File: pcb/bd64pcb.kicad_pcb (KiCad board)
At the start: 2 copper layers, 266.7 x 95.2 mm, 245 parts, among them J1 USB_C_Receptacle_USB2.0, SW1 SW_Push, U1 ATmega32U4-MU, U2 MCP23017_ML, U3 IS31FL3733-QF, Y1 16MHz

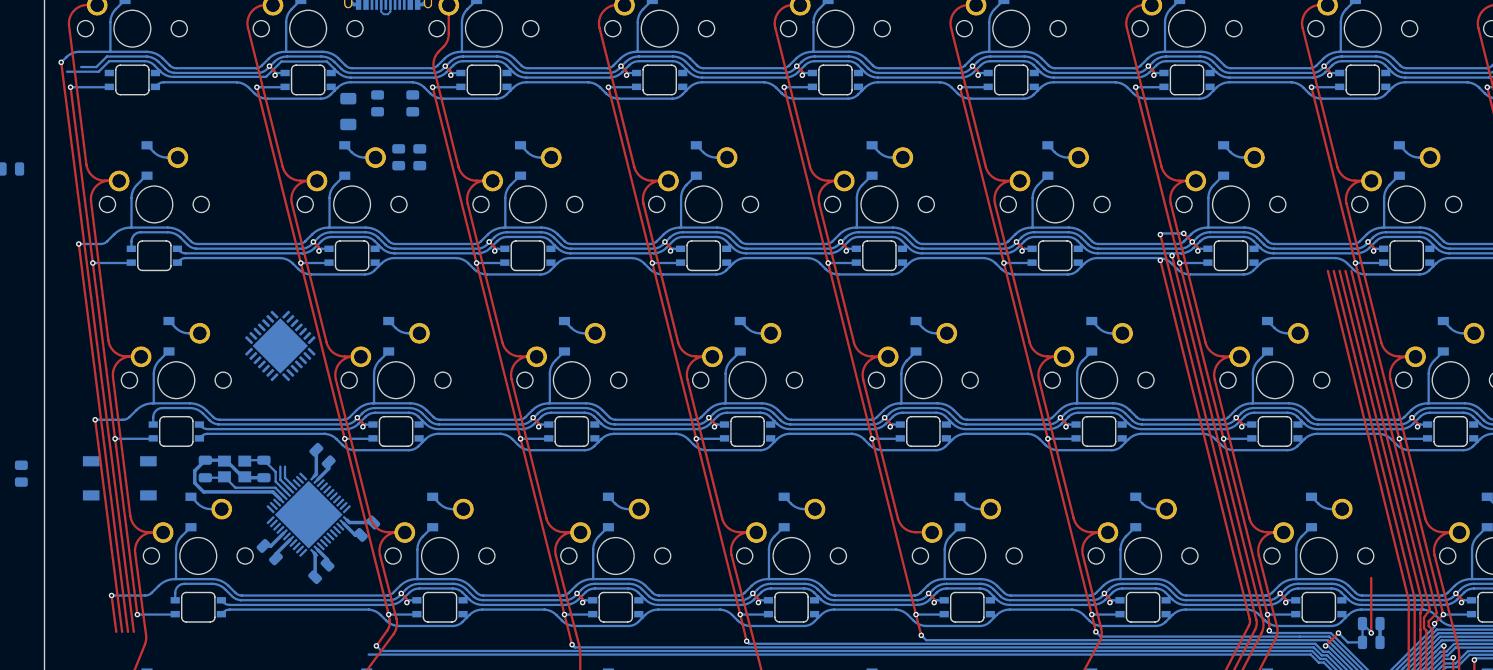
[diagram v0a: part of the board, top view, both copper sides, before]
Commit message: IIC lines from ISSI
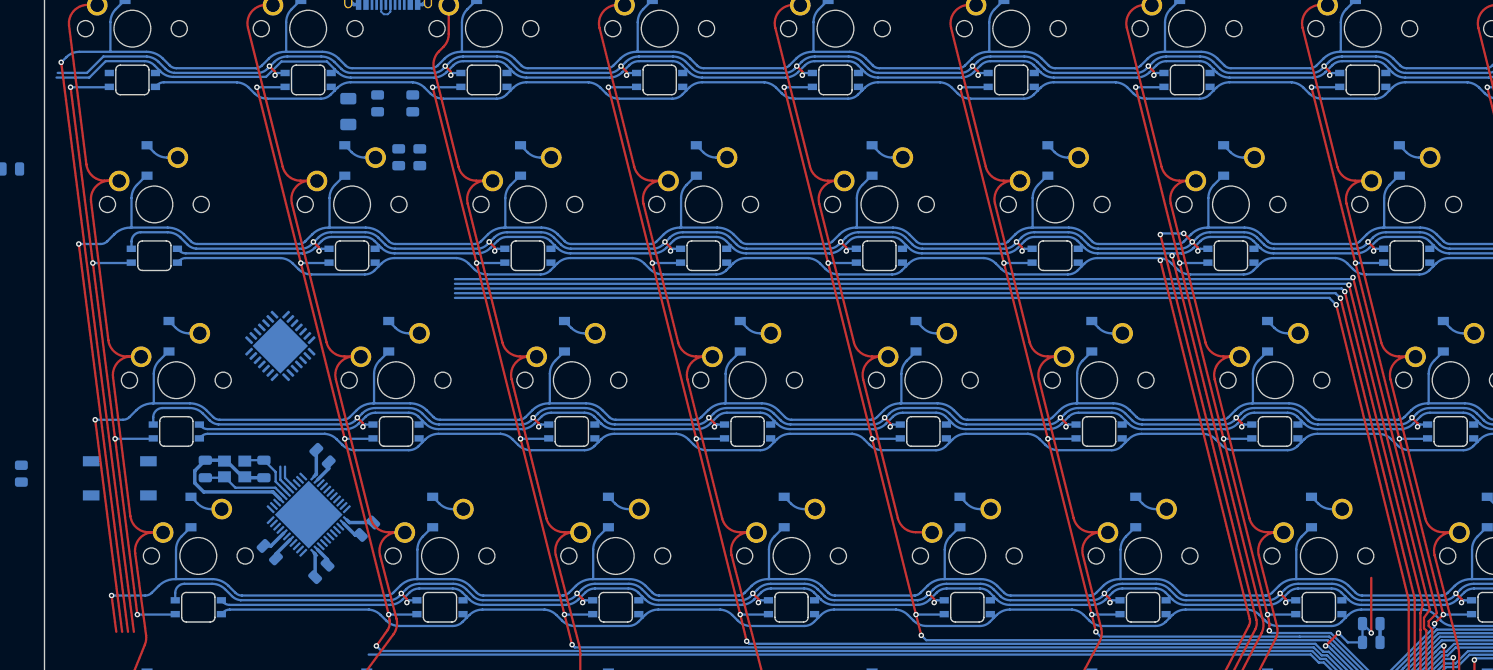
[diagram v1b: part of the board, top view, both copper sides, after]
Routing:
- net SDA: track 57.8 -> 154.4 mm, vias 1 -> 2
- net SCL: track 57.5 -> 152.9 mm, vias 1 -> 2
- net INTB: track 55.5 -> 149.8 mm, vias 1 -> 2
- net SDB: track 55.8 -> 149.0 mm, vias 1 -> 2
- net IICRST: track 56.3 -> 148.3 mm, vias 1 -> 2
- net SW3: track 342.3 -> 345.1 mm
- net SW1: track 322.1 -> 323.5 mm

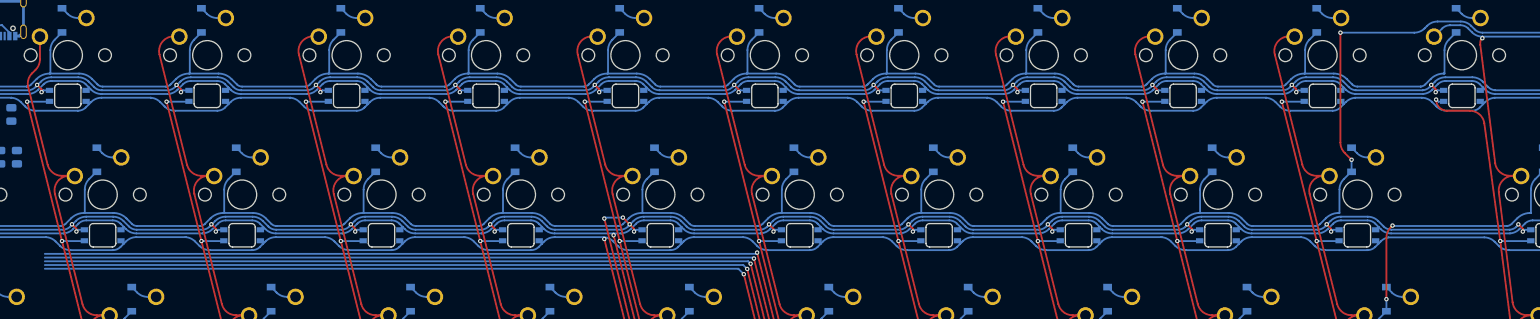
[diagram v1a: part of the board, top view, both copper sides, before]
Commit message: routing switch cols
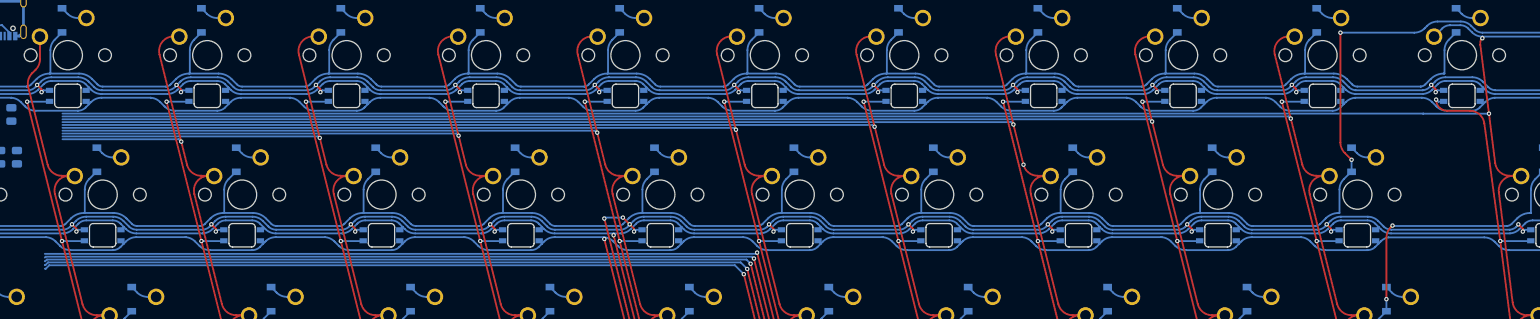
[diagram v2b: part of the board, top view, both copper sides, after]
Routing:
- net col12: track 89.9 -> 284.8 mm, vias 1 -> 2
- net col11: track 113.1 -> 281.1 mm, vias 1 -> 2
- net col10: track 109.0 -> 258.0 mm, vias 1 -> 2
- net col9: track 104.1 -> 234.2 mm, vias 1 -> 3
- net col8: track 99.5 -> 210.5 mm, vias 1 -> 2
- net col7: track 93.7 -> 185.8 mm, vias 0 -> 1
- net col6: track 94.5 -> 167.7 mm, vias 0 -> 1
- net col5: track 94.6 -> 148.8 mm, vias 0 -> 1
- net col4: track 72.5 -> 107.7 mm, vias 0 -> 1
- net col3: track 101.8 -> 118.1 mm, vias 1 -> 2

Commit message: finna delete mcp
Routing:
- net SW9: track 400.4 -> 416.7 mm
- net SW8: track 366.4 -> 381.1 mm, vias 2 -> 4
- net SW7: track 370.5 -> 378.2 mm, vias 2 -> 4
- net SW12: track 380.4 -> 385.7 mm, vias 32 -> 33
- net SW3: track 345.1 -> 348.0 mm, vias 30 -> 33
- net SW6: track 424.3 -> 426.2 mm, vias 33 -> 34
- net SW1: track 323.5 -> 321.8 mm, vias 0 -> 1
- net SW5: track 390.8 -> 392.1 mm, vias 2 -> 3
- net SW2: track 309.9 -> 309.1 mm, vias 0 -> 1
- net SW4: track 393.4 -> 394.2 mm, vias 2 -> 3

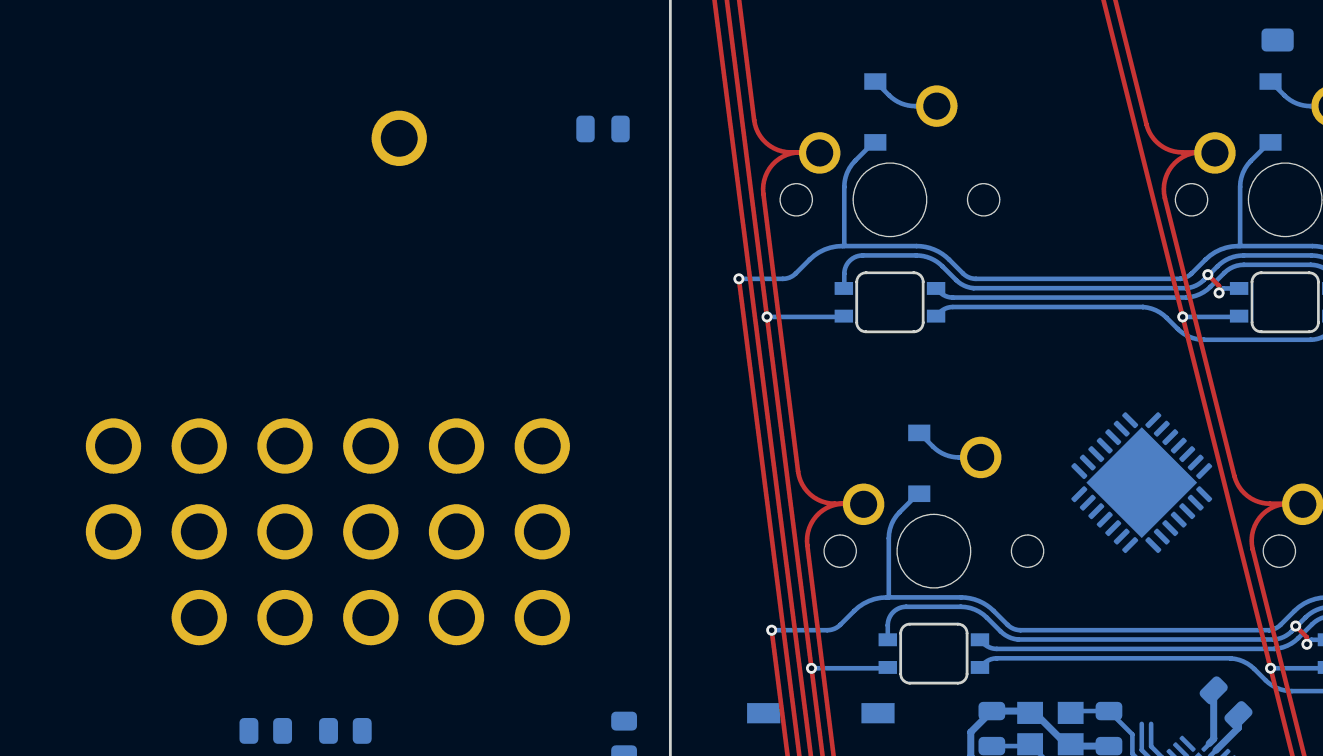
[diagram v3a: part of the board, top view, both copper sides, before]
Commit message: mcp delet
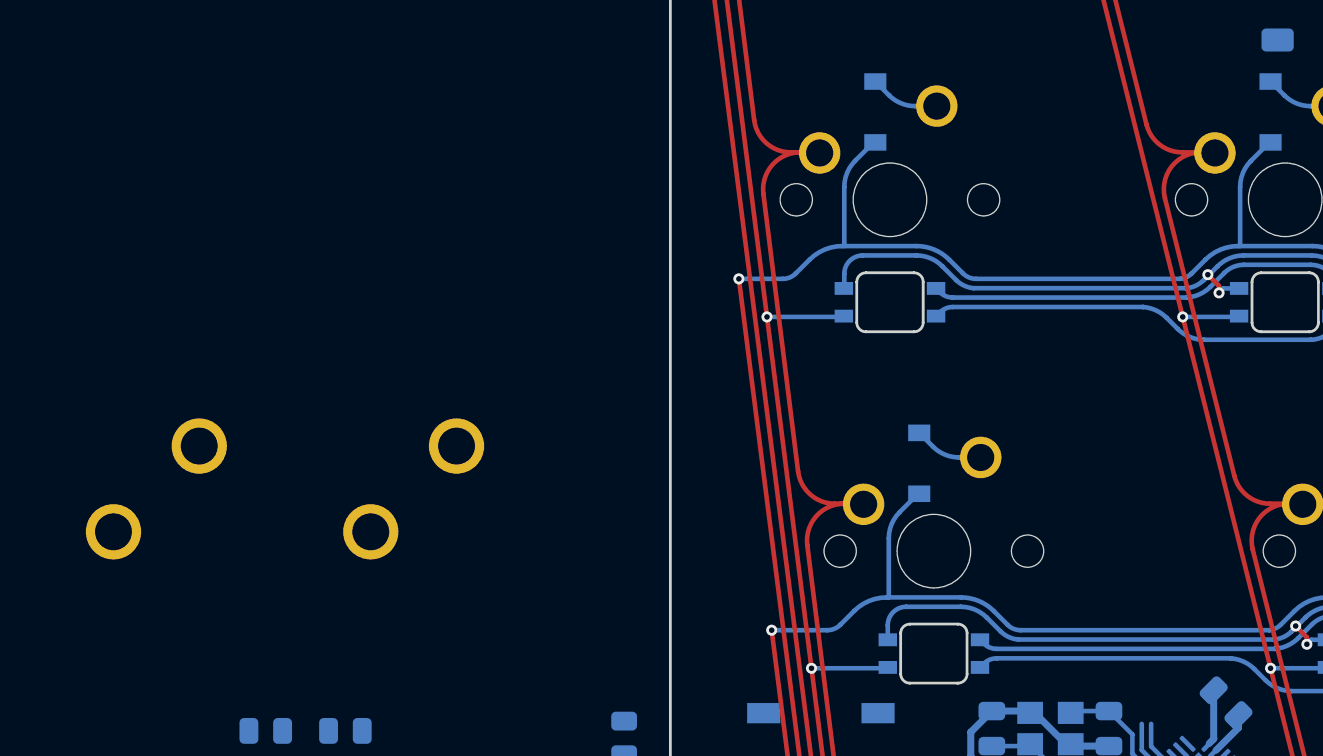
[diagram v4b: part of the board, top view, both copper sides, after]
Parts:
- removed C8: 1uF, Capacitor_SMD:C_0805_2012Metric
- removed TP1, TP10, TP11, TP12, TP13, TP14, TP15, TP16, TP17, TP18, TP2, TP4, TP6, TP8: TestPoint, TestPoint:TestPoint_Plated_Hole_D2.0mm
- removed U2: MCP23017_ML, Package_DFN_QFN:QFN-28-1EP_6x6mm_P0.65mm_EP4.25x4.25mm
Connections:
- U1 pad 21: unconnected-(U1-Pad21) -> row0
- U1 pad 22: unconnected-(U1-Pad22) -> row2
- U1 pad 25: unconnected-(U1-Pad25) -> row1
- U1 pad 26: unconnected-(U1-Pad26) -> row3
- U1 pad 27: unconnected-(U1-Pad27) -> row4

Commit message: sw1-3 routed
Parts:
- TP3, TP5, TP7, TP9: footprint TestPoint:TestPoint_Plated_Hole_D2.0mm -> TestPoint:TestPoint_Pad_D1.5mm
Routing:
- net SW2: track 309.1 -> 508.7 mm, vias 1 -> 4
- net SW1: track 321.8 -> 514.8 mm, vias 1 -> 4
- net SW3: track 348.0 -> 536.5 mm, vias 33 -> 36
- net CS1: track 183.4 -> 213.4 mm, vias 4 -> 5
- net row4: track 351.0 -> 350.5 mm, vias 2 -> 3

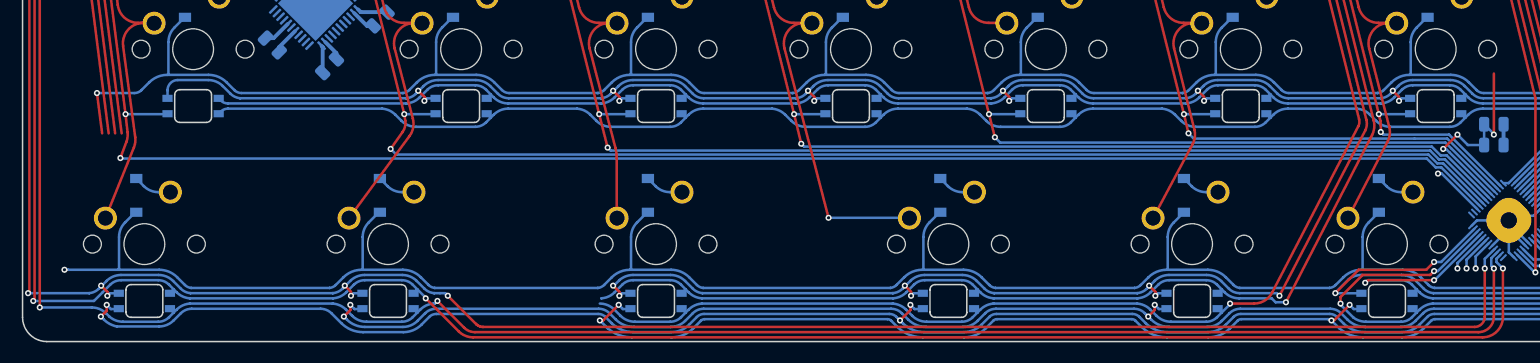
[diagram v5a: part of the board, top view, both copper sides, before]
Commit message: led SW pins routed
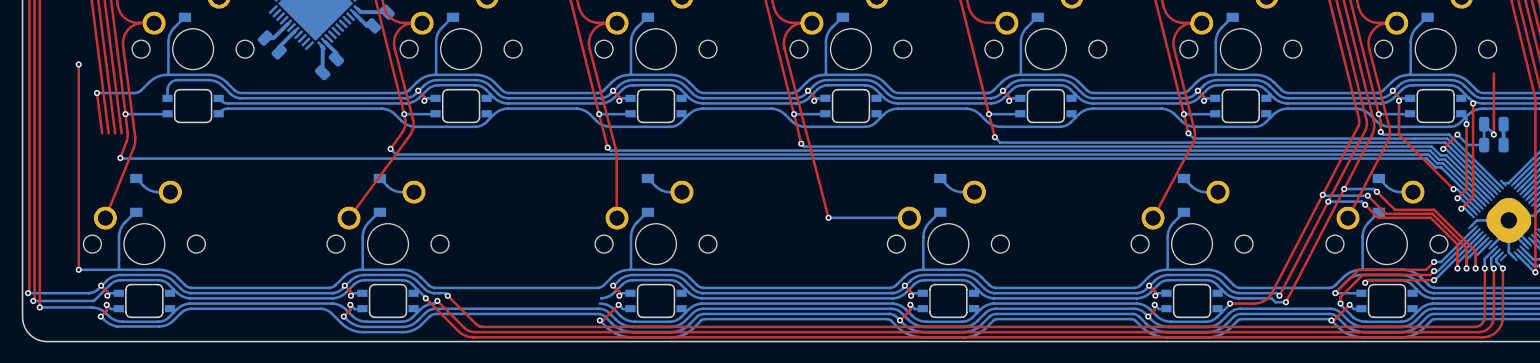
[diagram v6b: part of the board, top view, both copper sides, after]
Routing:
- net row4: track 350.5 -> 369.2 mm, vias 3 -> 4
- net SW5: track 392.1 -> 410.3 mm, vias 3 -> 5
- net SW4: track 394.2 -> 411.3 mm, vias 3 -> 5
- net SW6: track 426.2 -> 442.9 mm, vias 34 -> 36
- net SW10: track 348.3 -> 361.1 mm, vias 2 -> 4
- net SW11: track 350.0 -> 360.5 mm, vias 2 -> 4
- net SW12: track 385.7 -> 394.4 mm

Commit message: cleaning up loose ends
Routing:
- net GND: track 113.1 -> 177.6 mm
- net +5V: track 128.2 -> 192.5 mm
- net row3: track 350.2 -> 388.6 mm
- net row2: track 368.8 -> 388.0 mm
- net SW11: track 360.5 -> 351.0 mm
- net SW5: track 410.3 -> 400.8 mm
- net SW10: track 361.1 -> 351.7 mm
- net SW4: track 411.3 -> 401.9 mm
- net SW12: track 394.4 -> 391.2 mm, vias 33 -> 31
- net SW6: track 442.9 -> 439.8 mm, vias 36 -> 34
- net CS14: track 379.4 -> 378.7 mm

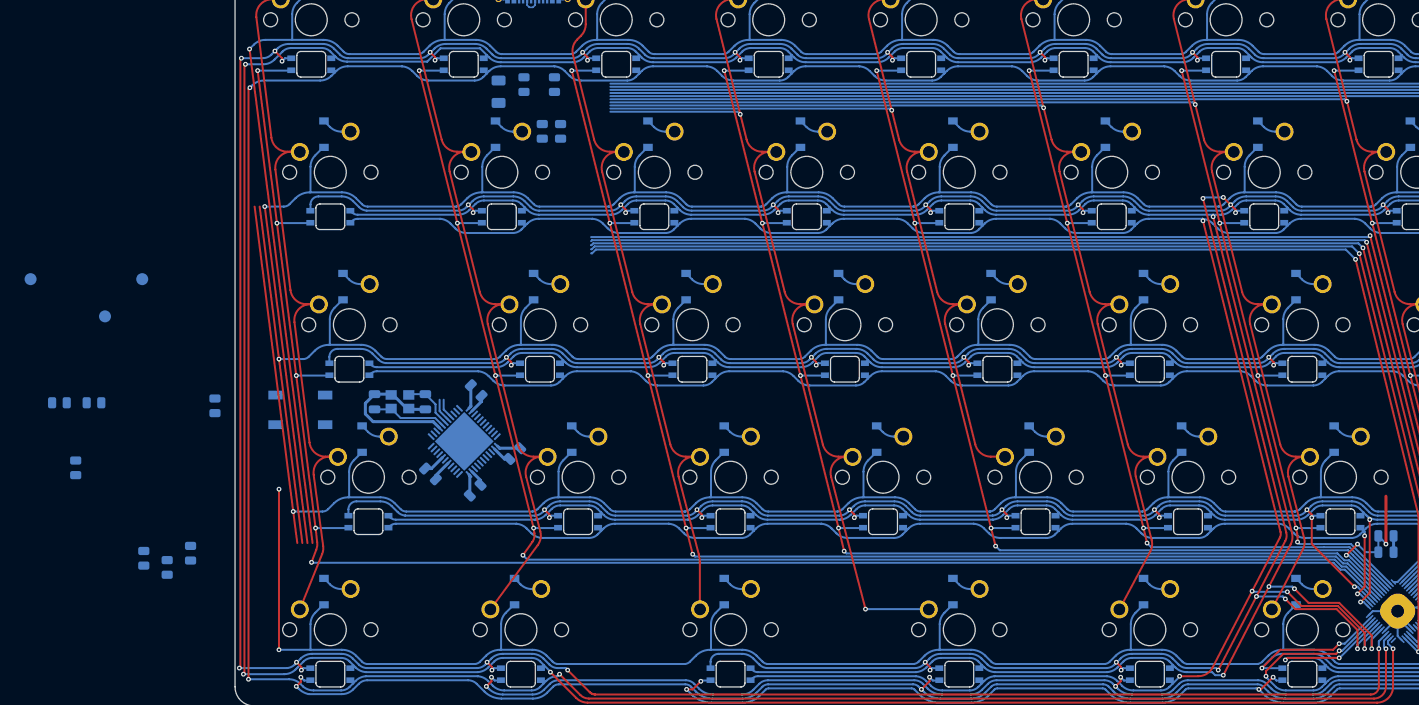
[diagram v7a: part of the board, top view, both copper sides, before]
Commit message: switch rows routed
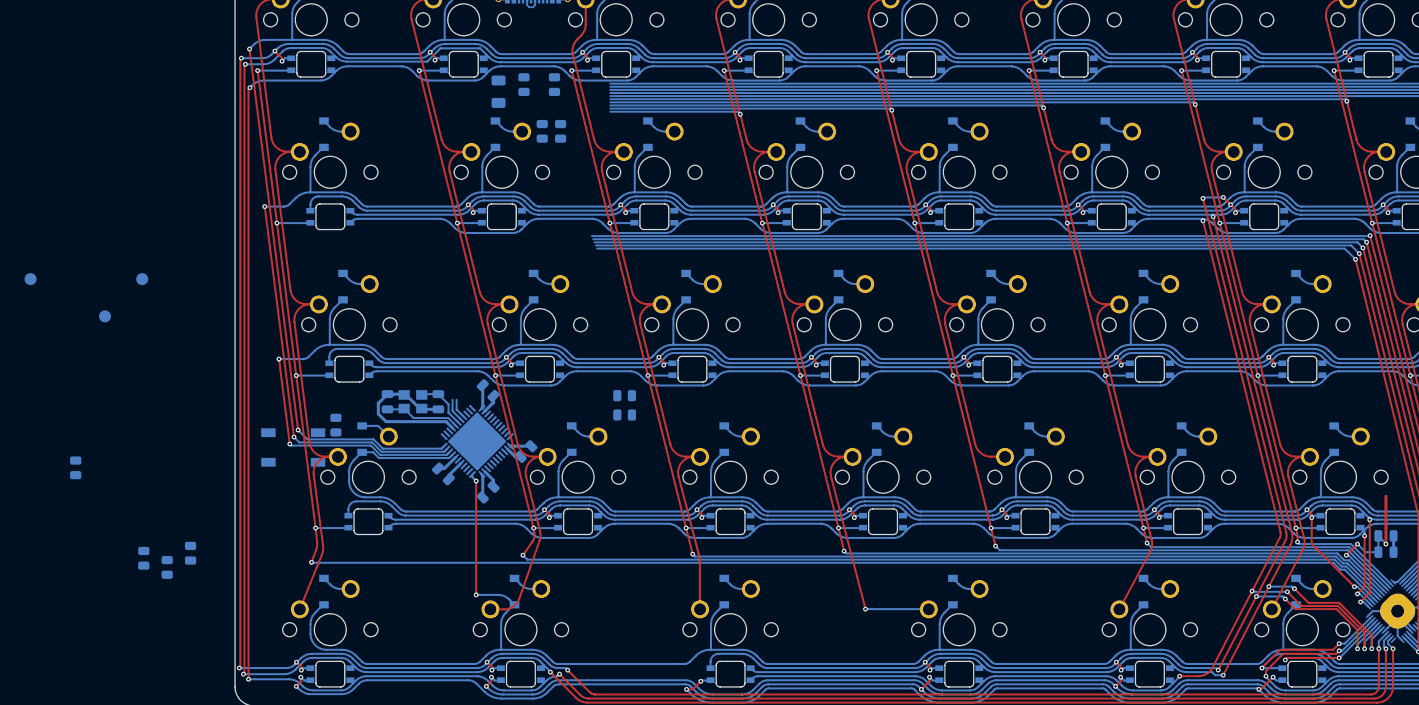
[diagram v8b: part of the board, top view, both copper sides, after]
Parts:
- moved R11 70.6 mm to (63.8, 101.0)
- moved R10 66.3 mm to (63.8, 98.6)
- moved R3 15.3 mm to (27.7, 102.2), turned to 90 degrees
- moved SW1 4.78 mm to (22.4, 105.0)
- moved C4 1.64 mm to (46.7, 110.6)
- moved C3 1.62 mm to (41.1, 108.3)
- moved C5 1.62 mm to (40.5, 99.3)
- moved C6 1.62 mm to (34.1, 99.3)
- moved U1 1.62 mm to (45.3, 104.3)
- moved Y1 1.62 mm to (37.3, 99.3)
- moved C1 1.49 mm to (46.7, 97.9)
- moved C2 1.42 mm to (51.4, 105.5)
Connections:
- U1 pad 1: unconnected-(U1-Pad1) -> row4
- U1 pad 10: unconnected-(U1-Pad10) -> row1
- U1 pad 11: unconnected-(U1-Pad11) -> row0
- U1 pad 21: row0 -> unconnected-(U1-Pad21)
- U1 pad 22: row2 -> unconnected-(U1-Pad22)
- U1 pad 25: row1 -> unconnected-(U1-Pad25)
- U1 pad 26: row3 -> unconnected-(U1-Pad26)
- U1 pad 27: row4 -> unconnected-(U1-Pad27)
- U1 pad 8: unconnected-(U1-Pad8) -> row3
- U1 pad 9: unconnected-(U1-Pad9) -> row2
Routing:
- net row3: track 388.6 -> 349.6 mm, vias 3 -> 2
- net row2: track 388.0 -> 377.1 mm, vias 3 -> 4
- net row1: track 403.3 -> 410.0 mm, vias 3 -> 4
- net row0: track 390.6 -> 395.7 mm, vias 1 -> 2
- net row4: track 369.2 -> 364.7 mm
- net col1: track 95.6 -> 96.8 mm
- net IICRST: track 148.7 -> 147.8 mm
- net SDB: track 149.3 -> 148.6 mm
